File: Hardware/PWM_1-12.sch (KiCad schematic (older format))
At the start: 0 parts

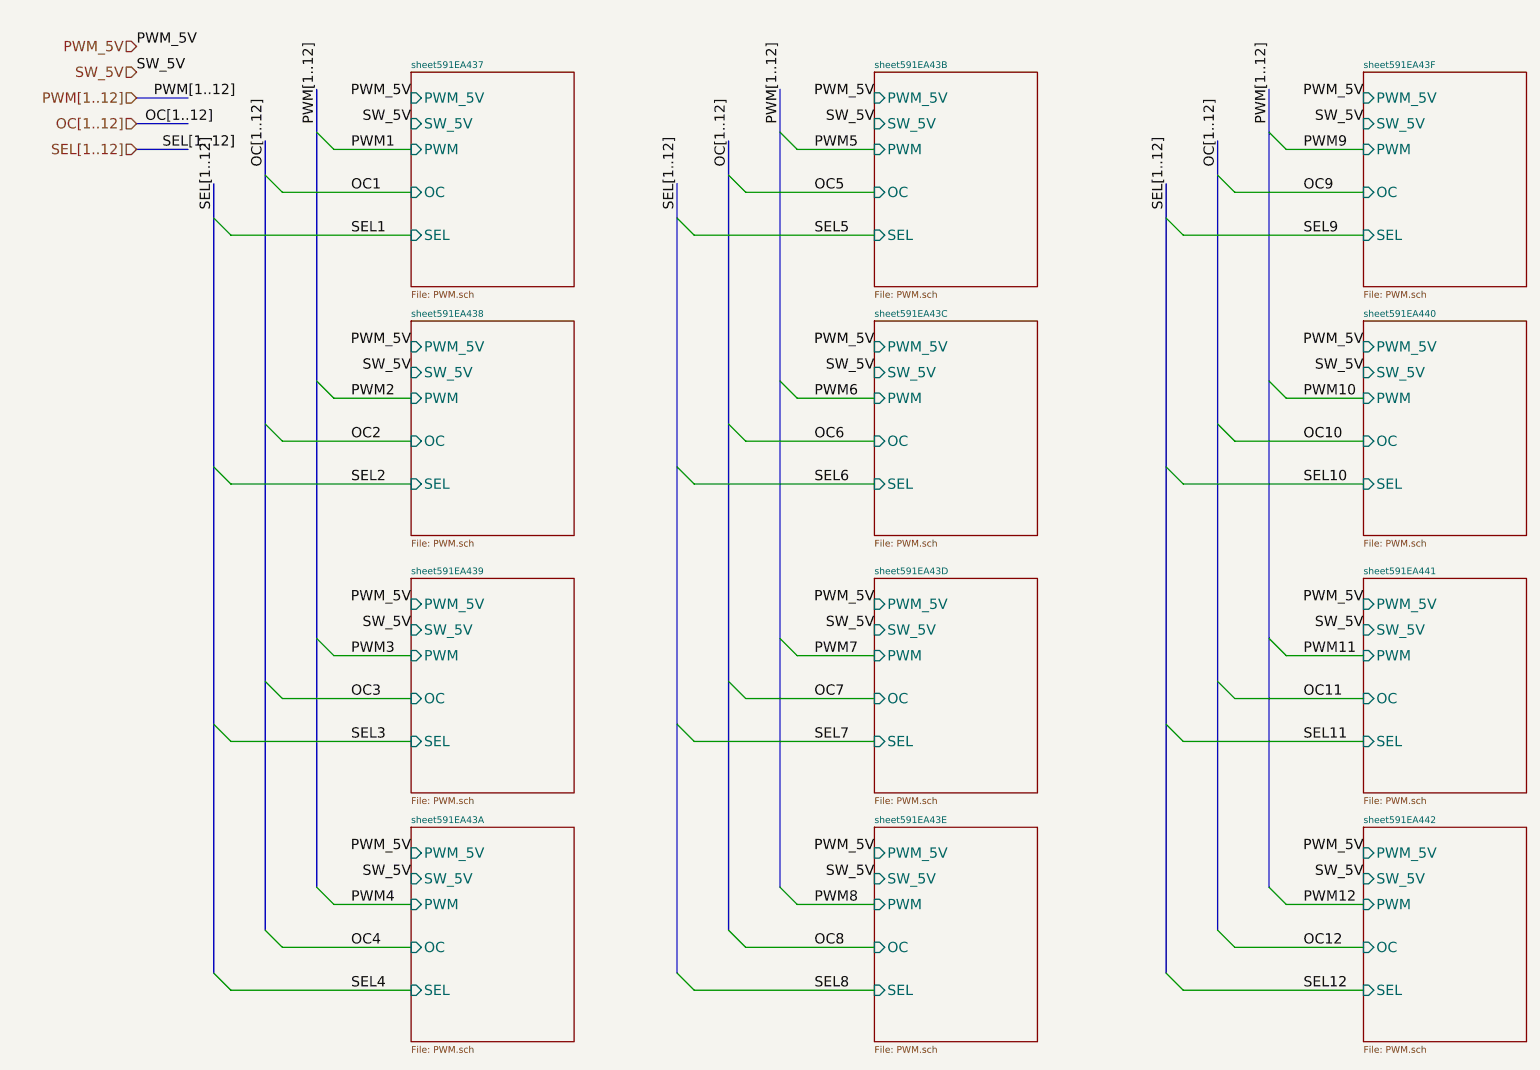
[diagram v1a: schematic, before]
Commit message: Restarted work
Removed OC and SEL busses. Still need to add clocks.
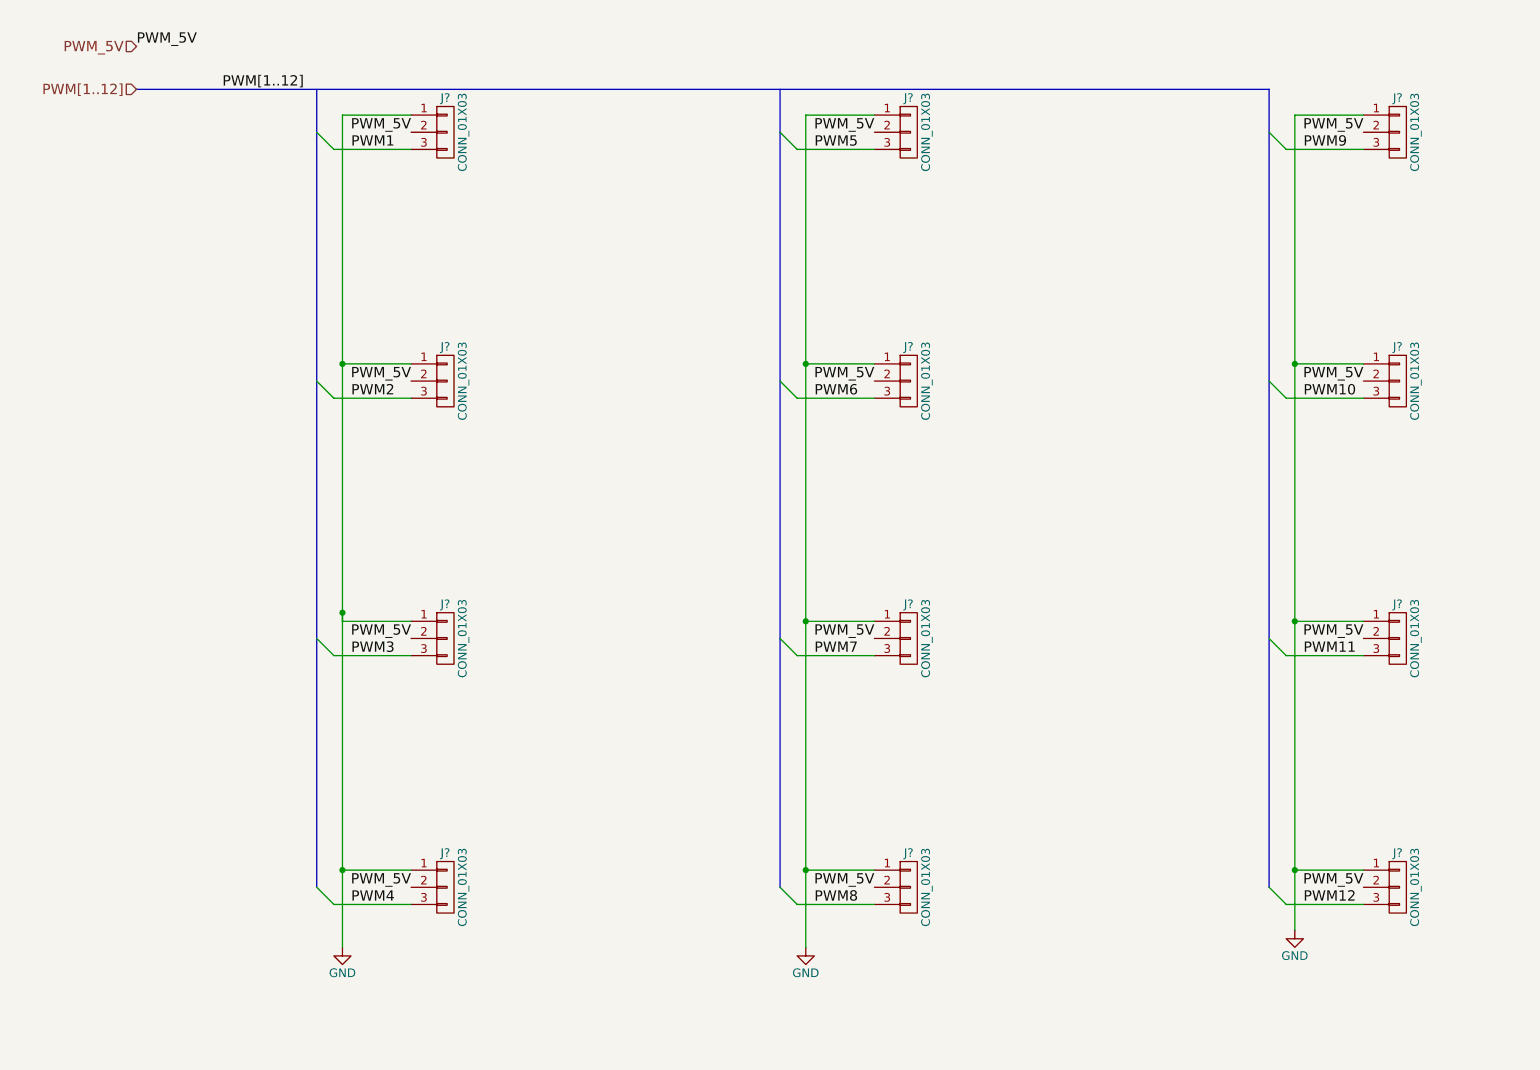
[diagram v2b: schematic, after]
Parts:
- added J? (x12): CONN_01X03, symbol CONN_01X03
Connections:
- net PWM1: now also J?.3 (P3)
- net PWM10: now also J?.3 (P3)
- net PWM11: now also J?.3 (P3)
- net PWM12: now also J?.3 (P3)
- net PWM2: now also J?.3 (P3)
- net PWM3: now also J?.3 (P3)
- net PWM4: now also J?.3 (P3)
- net PWM5: now also J?.3 (P3)
- net PWM6: now also J?.3 (P3)
- net PWM7: now also J?.3 (P3)
- net PWM8: now also J?.3 (P3)
- net PWM9: now also J?.3 (P3)
- net PWM_5V: now also J?.2 (P2), J?.2 (P2), J?.2 (P2), J?.2 (P2), J?.2 (P2), J?.2 (P2), J?.2 (P2), J?.2 (P2), J?.2 (P2), J?.2 (P2), J?.2 (P2), J?.2 (P2)
- new net GND: J?.1 (P1), J?.1 (P1), J?.1 (P1), J?.1 (P1), J?.1 (P1), J?.1 (P1), J?.1 (P1), J?.1 (P1), J?.1 (P1), J?.1 (P1), J?.1 (P1), J?.1 (P1)

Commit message: Placement and preminiary routing
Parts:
- gave numbers to parts that had none: 12
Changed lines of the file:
@@
 PWM_5V
 $Comp
-L CONN_01X03 J?
+L CONN_01X03 J2
 U 1 1 597DAC0F
 P 2900 1150
-F 0 "J?" H 2900 1350 50  0000 C CNN
+F 0 "J2" H 2900 1350 50  0000 C CNN
 F 1 "CONN_01X03" V 3000 1150 50  0000 C CNN
 F 2 "" H 2900 1150 50  0001 C CNN
@@
 $EndComp
 $Comp
-L CONN_01X03 J?
+L CONN_01X03 J3
 U 1 1 597DAC47
 P 2900 2600
-F 0 "J?" H 2900 2800 50  0000 C CNN
+F 0 "J3" H 2900 2800 50  0000 C CNN
 F 1 "CONN_01X03" V 3000 2600 50  0000 C CNN
 F 2 "" H 2900 2600 50  0001 C CNN
@@
 $EndComp
 $Comp
-L CONN_01X03 J?
+L CONN_01X03 J4
 U 1 1 597DAC6B
 P 2900 4100
-F 0 "J?" H 2900 4300 50  0000 C CNN
+F 0 "J4" H 2900 4300 50  0000 C CNN
 F 1 "CONN_01X03" V 3000 4100 50  0000 C CNN
 F 2 "" H 2900 4100 50  0001 C CNN
@@
 $EndComp
 $Comp
-L CONN_01X03 J?
+L CONN_01X03 J5
 U 1 1 597DAC90
 P 2900 5550
-F 0 "J?" H 2900 5750 50  0000 C CNN
+F 0 "J5" H 2900 5750 50  0000 C CNN
 F 1 "CONN_01X03" V 3000 5550 50  0000 C CNN
 F 2 "" H 2900 5550 50  0001 C CNN
@@
 $EndComp
 $Comp
-L CONN_01X03 J?
+L CONN_01X03 J6
 U 1 1 597DACBD
 P 5600 1150
-F 0 "J?" H 5600 1350 50  0000 C CNN
+F 0 "J6" H 5600 1350 50  0000 C CNN
 F 1 "CONN_01X03" V 5700 1150 50  0000 C CNN
 F 2 "" H 5600 1150 50  0001 C CNN
@@
 $EndComp
 $Comp
-L CONN_01X03 J?
+L CONN_01X03 J7
 U 1 1 597DAD07
 P 5600 2600
-F 0 "J?" H 5600 2800 50  0000 C CNN
+F 0 "J7" H 5600 2800 50  0000 C CNN
 F 1 "CONN_01X03" V 5700 2600 50  0000 C CNN
 F 2 "" H 5600 2600 50  0001 C CNN
@@
 $EndComp
 $Comp
-L CONN_01X03 J?
+L CONN_01X03 J8
 U 1 1 597DAD31
 P 5600 4100
-F 0 "J?" H 5600 4300 50  0000 C CNN
+F 0 "J8" H 5600 4300 50  0000 C CNN
 F 1 "CONN_01X03" V 5700 4100 50  0000 C CNN
 F 2 "" H 5600 4100 50  0001 C CNN
@@
 $EndComp
 $Comp
-L CONN_01X03 J?
+L CONN_01X03 J9
 U 1 1 597DAD60
 P 5600 5550
-F 0 "J?" H 5600 5750 50  0000 C CNN
+F 0 "J9" H 5600 5750 50  0000 C CNN
 F 1 "CONN_01X03" V 5700 5550 50  0000 C CNN
 F 2 "" H 5600 5550 50  0001 C CNN
@@
 $EndComp
 $Comp
-L CONN_01X03 J?
+L CONN_01X03 J10
 U 1 1 597DAD94
 P 8450 1150
-F 0 "J?" H 8450 1350 50  0000 C CNN
+F 0 "J10" H 8450 1350 50  0000 C CNN
 F 1 "CONN_01X03" V 8550 1150 50  0000 C CNN
 F 2 "" H 8450 1150 50  0001 C CNN
@@
 $EndComp
 $Comp
-L CONN_01X03 J?
+L CONN_01X03 J11
 U 1 1 597DADE4
 P 8450 2600
-F 0 "J?" H 8450 2800 50  0000 C CNN
+F 0 "J11" H 8450 2800 50  0000 C CNN
 F 1 "CONN_01X03" V 8550 2600 50  0000 C CNN
 F 2 "" H 8450 2600 50  0001 C CNN
@@
 $EndComp
 $Comp
-L CONN_01X03 J?
+L CONN_01X03 J12
 U 1 1 597DAE21
 P 8450 4100
-F 0 "J?" H 8450 4300 50  0000 C CNN
+F 0 "J12" H 8450 4300 50  0000 C CNN
 F 1 "CONN_01X03" V 8550 4100 50  0000 C CNN
 F 2 "" H 8450 4100 50  0001 C CNN
@@
 $EndComp
 $Comp
-L CONN_01X03 J?
+L CONN_01X03 J13
 U 1 1 597DAE61
 P 8450 5550
-F 0 "J?" H 8450 5750 50  0000 C CNN
+F 0 "J13" H 8450 5750 50  0000 C CNN
 F 1 "CONN_01X03" V 8550 5550 50  0000 C CNN
 F 2 "" H 8450 5550 50  0001 C CNN
@@
 $EndComp
 $Comp
-L GND #PWR?
+L GND #PWR3
 U 1 1 597DB10B
 P 2300 5900
-F 0 "#PWR?" H 2300 5650 50  0001 C CNN
+F 0 "#PWR3" H 2300 5650 50  0001 C CNN
 F 1 "GND" H 2300 5750 50  0000 C CNN
 F 2 "" H 2300 5900 50  0001 C CNN
@@
 Connection ~ 2300 5450
 $Comp
-L GND #PWR?
+L GND #PWR4
 U 1 1 597DB1D3
 P 5000 5900
-F 0 "#PWR?" H 5000 5650 50  0001 C CNN
+F 0 "#PWR4" H 5000 5650 50  0001 C CNN
 F 1 "GND" H 5000 5750 50  0000 C CNN
 F 2 "" H 5000 5900 50  0001 C CNN
@@
 $EndComp
 $Comp
-L GND #PWR?
+L GND #PWR5
 U 1 1 597DB202
 P 7850 5800
-F 0 "#PWR?" H 7850 5550 50  0001 C CNN
+F 0 "#PWR5" H 7850 5550 50  0001 C CNN
 F 1 "GND" H 7850 5650 50  0000 C CNN
 F 2 "" H 7850 5800 50  0001 C CNN

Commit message: Ported to kicad5
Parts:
- J10, J11, J12, J13, J2, J3, J4, J5, J6, J7, J8, J9: symbol CONN_01X03 -> conn:CONN_01X03
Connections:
- net GND: no longer J4.1 (P1)
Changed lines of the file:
@@
-EESchema Schematic File Version 2
-LIBS:ZeroPilot-rescue
-LIBS:WARG
-LIBS:power
-LIBS:device
-LIBS:transistors
-LIBS:conn
-LIBS:linear
-LIBS:regul
-LIBS:74xx
-LIBS:cmos4000
-LIBS:adc-dac
-LIBS:memory
-LIBS:xilinx
-LIBS:microcontrollers
-LIBS:dsp
-LIBS:microchip
-LIBS:analog_switches
-LIBS:motorola
-LIBS:texas
-LIBS:intel
-LIBS:audio
-LIBS:interface
-LIBS:digital-audio
-LIBS:philips
-LIBS:display
-LIBS:cypress
-LIBS:siliconi
-LIBS:opto
-LIBS:atmel
-LIBS:contrib
-LIBS:valves
+EESchema Schematic File Version 4
 LIBS:ZeroPilot-cache
-EELAYER 25 0
+EELAYER 29 0
 EELAYER END
 $Descr A4 11693 8268
@@
 Text Label 7900 5650 0    60   ~ 0
 PWM12
-Wire Bus Line
-	2150 900  2150 5550
 Wire Wire Line
 	2250 5650 2700 5650
@@
 Wire Wire Line
 	2250 1250 2700 1250
-Wire Bus Line
-	4850 900  4850 5550
 Wire Wire Line
 	4950 5650 5400 5650
@@
 Wire Wire Line
 	4950 1250 5400 1250
-Wire Bus Line
-	7700 900  7700 5550
 Wire Wire Line
 	7800 5650 8250 5650
@@
 PWM_5V
 $Comp
-L CONN_01X03 J2
+L conn:CONN_01X03 J2
 U 1 1 597DAC0F
 P 2900 1150
@@
 $EndComp
 $Comp
-L CONN_01X03 J3
+L conn:CONN_01X03 J3
 U 1 1 597DAC47
 P 2900 2600
@@
 $EndComp
 $Comp
-L CONN_01X03 J4
+L conn:CONN_01X03 J4
 U 1 1 597DAC6B
 P 2900 4100
@@
 $EndComp
 $Comp
-L CONN_01X03 J5
+L conn:CONN_01X03 J5
 U 1 1 597DAC90
 P 2900 5550
@@
 $EndComp
 $Comp
-L CONN_01X03 J6
+L conn:CONN_01X03 J6
 U 1 1 597DACBD
 P 5600 1150
@@
 $EndComp
 $Comp
-L CONN_01X03 J7
+L conn:CONN_01X03 J7
 U 1 1 597DAD07
 P 5600 2600
@@
 $EndComp
 $Comp
-L CONN_01X03 J8
+L conn:CONN_01X03 J8
 U 1 1 597DAD31
 P 5600 4100
@@
 $EndComp
 $Comp
-L CONN_01X03 J9
+L conn:CONN_01X03 J9
 U 1 1 597DAD60
 P 5600 5550
@@
 $EndComp
 $Comp
-L CONN_01X03 J10
+L conn:CONN_01X03 J10
 U 1 1 597DAD94
 P 8450 1150
@@
 $EndComp
 $Comp
-L CONN_01X03 J11
+L conn:CONN_01X03 J11
 U 1 1 597DADE4
 P 8450 2600
@@
 $EndComp
 $Comp
-L CONN_01X03 J12
+L conn:CONN_01X03 J12
 U 1 1 597DAE21
 P 8450 4100
@@
 $EndComp
 $Comp
-L CONN_01X03 J13
+L conn:CONN_01X03 J13
 U 1 1 597DAE61
 P 8450 5550
@@
 $EndComp
 $Comp
-L GND #PWR3
+L power:GND #PWR3
 U 1 1 597DB10B
 P 2300 5900
@@
 	2700 1050 2300 1050
 Wire Wire Line
-	2300 1050 2300 5900
+	2300 1050 2300 2500
 Wire Wire Line
 	2700 2500 2300 2500
@@
 Wire Wire Line
 	2700 4000 2300 4000
-Wire Wire Line
-	2300 4000 2300 3950
 Connection ~ 2300 3950
 Wire Wire Line
@@
 Connection ~ 2300 5450
 $Comp
-L GND #PWR4
+L power:GND #PWR4
 U 1 1 597DB1D3
 P 5000 5900
@@
 $EndComp
 $Comp
-L GND #PWR5
+L power:GND #PWR5
 U 1 1 597DB202
 P 7850 5800
@@
 $EndComp
 Wire Wire Line
-	7850 1050 7850 5800
+	7850 1050 7850 2500
 Wire Wire Line
 	7850 1050 8250 1050
@@
 	5400 4000 5000 4000
 Wire Wire Line
-	5000 1050 5000 5900
+	5000 1050 5000 2500
 Wire Wire Line
 	5400 1050 5000 1050
@@
 	5400 2500 5000 2500
 Connection ~ 5000 2500
+Wire Wire Line
+	2300 5450 2300 5900
+Wire Wire Line
+	7850 2500 7850 4000
+Wire Wire Line
+	7850 4000 7850 5450
+Wire Wire Line
+	7850 5450 7850 5800
+Wire Wire Line
+	5000 4000 5000 5450
+Wire Wire Line
+	5000 5450 5000 5900
+Wire Wire Line
+	5000 2500 5000 4000
+Wire Wire Line
+	2300 2500 2300 5450
+Wire Bus Line
+	2150 900  2150 5550
+Wire Bus Line
+	4850 900  4850 5550
+Wire Bus Line
+	7700 900  7700 5550
 $EndSCHEMATC
